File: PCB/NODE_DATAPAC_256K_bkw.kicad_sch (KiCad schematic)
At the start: 28 parts, among them J1 Conn_02x20_Odd_Even, U1 74161, U10 62256, U2 74161, U3 74161, U4 74138, U5 74138, U6 74374, U7 62256, U8 62256, U9 62256

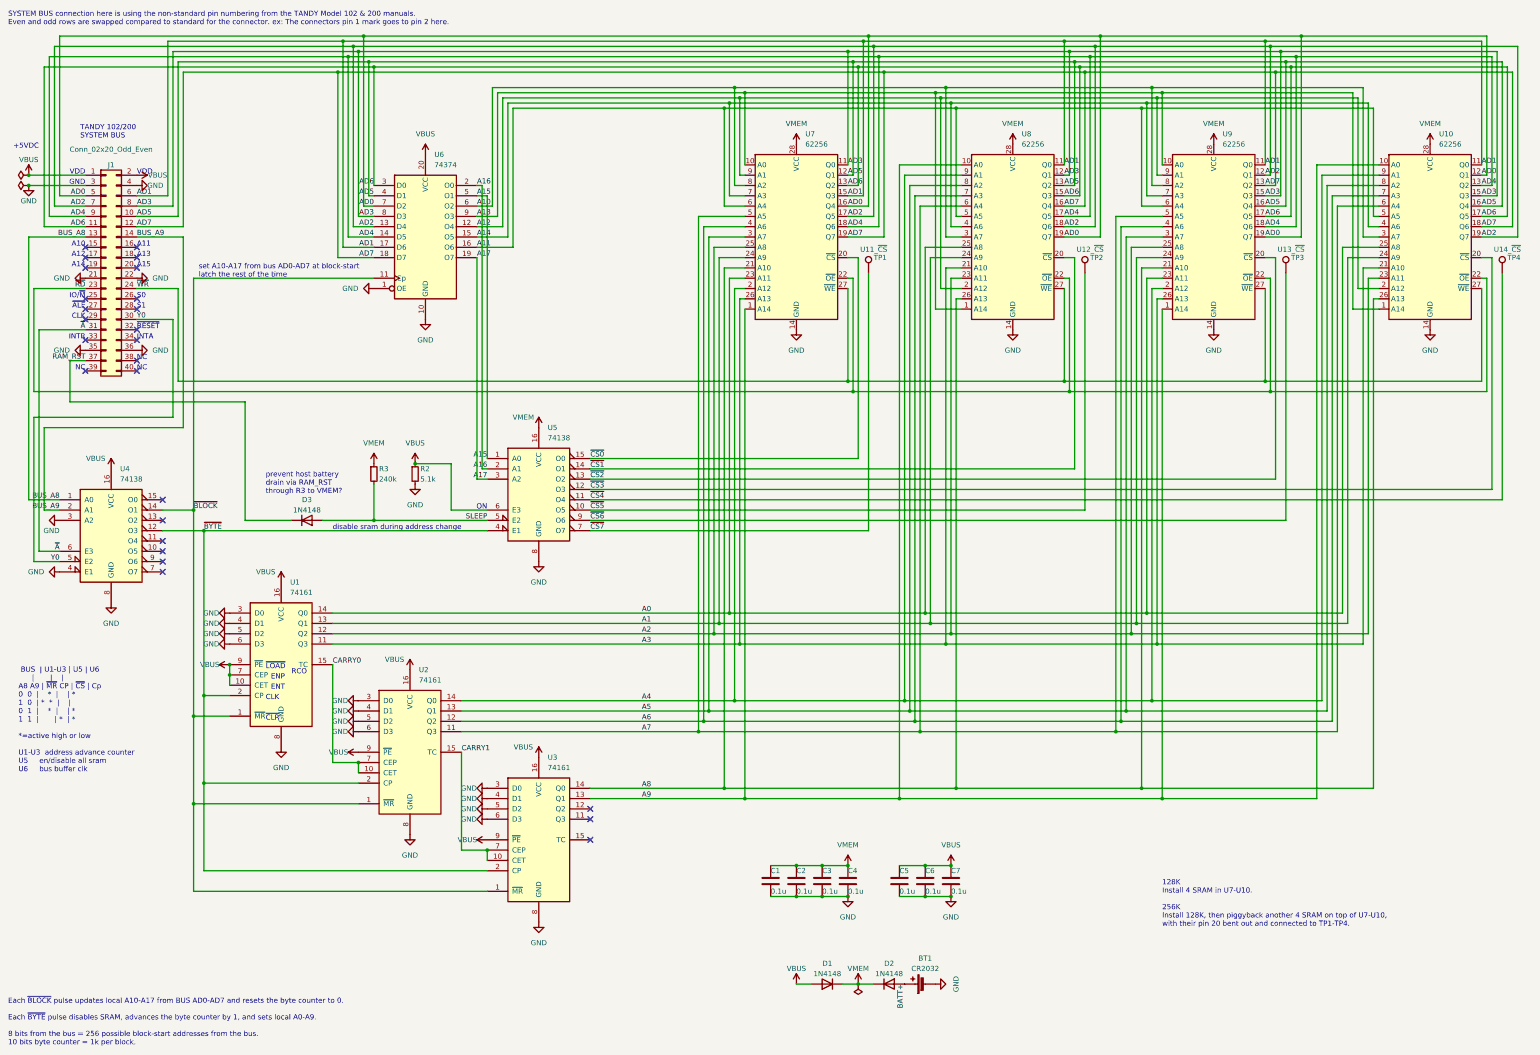
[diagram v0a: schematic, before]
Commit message: convert wires to busses in bkw sch
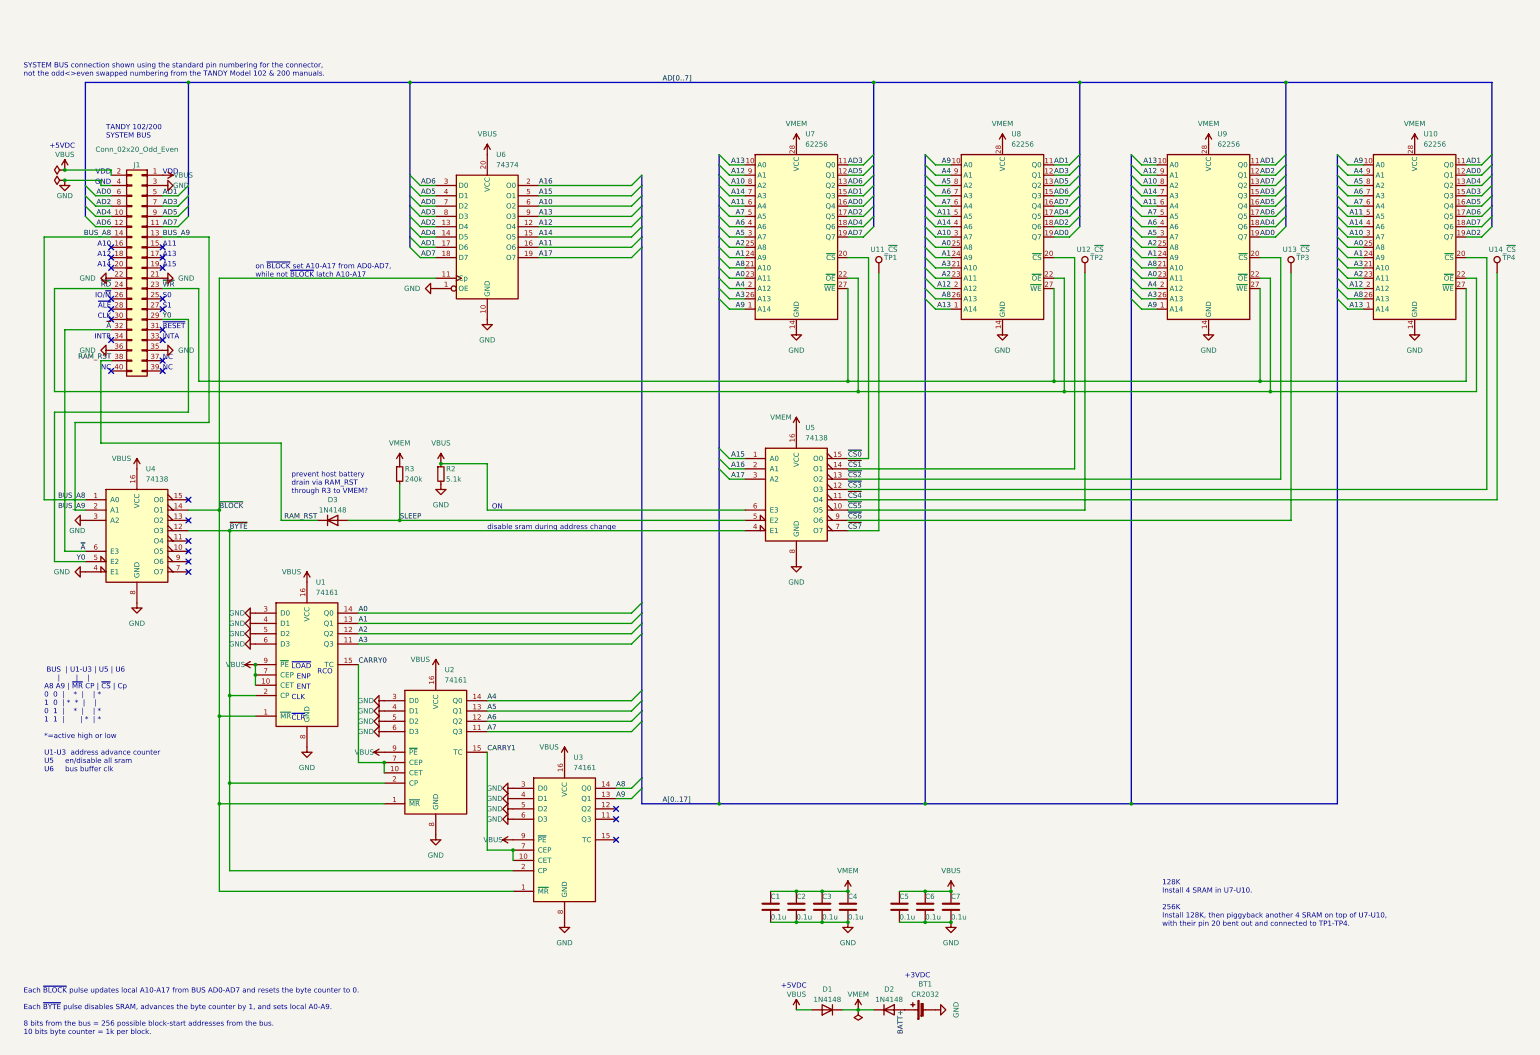
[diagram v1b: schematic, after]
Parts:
- J1: footprint 000_LOCAL:IDC_to_board_2x20_flipped -> 000_LOCAL:IDC_to_board_2x20
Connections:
- net AD0: now also J1.6 (Pin_6); no longer J1.5 (Pin_5)
- net AD1: now also J1.5 (Pin_5); no longer J1.6 (Pin_6)
- net AD2: now also J1.8 (Pin_8); no longer J1.7 (Pin_7)
- net AD3: now also J1.7 (Pin_7); no longer J1.8 (Pin_8)
- net AD4: now also J1.10 (Pin_10); no longer J1.9 (Pin_9)
- net AD5: now also J1.9 (Pin_9); no longer J1.10 (Pin_10)
- net AD6: now also J1.12 (Pin_12); no longer J1.11 (Pin_11)
- net AD7: now also J1.11 (Pin_11); no longer J1.12 (Pin_12)
- net BUS_A8: now also J1.14 (Pin_14); no longer J1.13 (Pin_13)
- net BUS_A9: now also J1.13 (Pin_13); no longer J1.14 (Pin_14)
- net RAM_RST: now also J1.38 (Pin_38); no longer J1.37 (Pin_37)
- net Y0: now also J1.29 (Pin_29); no longer J1.30 (Pin_30)
- net ~{A}: now also J1.32 (Pin_32); no longer J1.31 (Pin_31)
- net ~{RD}: now also J1.24 (Pin_24); no longer J1.23 (Pin_23)
- net ~{WR}: now also J1.23 (Pin_23); no longer J1.24 (Pin_24)
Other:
- note added: "+3VDC"
- note added: "SYSTEM BUS connection shown using the standard pin numbering for the connector, not the odd<>even swapped numbering from the TANDY Model 102 & 200 manuals."
- note added: "on ~{BLOCK} set A10-A17 from AD0-AD7, while not ~{BLOCK} latch A10-A17"
- note removed: "SYSTEM BUS connection here is using the non-standard pin numbering from the TANDY Model 102 & 200 manuals. Even and odd rows are swapped compared to standard for the connector. ex: The connectors pin 1 mark goes to pin 2 here."
- note removed: "set A10-A17 from bus AD0-AD7 at block-start latch the rest of the time"
- title: NODE DATAPAC 256K bkw0 -> NODE DATAPAC 256K bkw
- moved on the sheet: BT1, C1, C2, C3, C4, C5, C6, C7, D1, D2, D3, J1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

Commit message: schematic notes
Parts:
- C1, C2, C3, C4, C5, C6, C7: value 0.1u -> 1u
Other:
- note added: "BUS | U1-U3 | U5 | U6 | | | A8 A9 | ~{MR} CP | ~{CS} | Cp 0 0 | * | | * 1 0 | * * | | 0 1 | * | | * 1 1 | | * | * *=active, whether high or low U1-U3 byte address increment U5 enable/disable sram U6 block address latch"
- note added: "While ~{BLOCK} is low, A0-A9 are set to 0, A10-A17 are copied from AD0-AD7. While ~{BLOCK} is high, A10-A17 are latched and held. While ~{BYTE} is low, SRAM is enabled. When ~{BYTE} goes from low to high, A0-A9 are incremented by 1. While ~{BYTE} is high, SRAM is disabled. A0-A9 = 10 bits byte number = 1024 bytes per block AD0-AD7 -> A10-A17 = 8 bits block number = 256 blocks"
- note removed: "BUS | U1-U3 | U5 | U6 | | | A8 A9 | ~{MR} CP | ~{CS} | Cp 0 0 | * | | * 1 0 | * * | | 0 1 | * | | * 1 1 | | * | * *=active high or low U1-U3 address advance counter U5 en/disable all sram U6 bus buffer clk"
- note removed: "Each ~{BLOCK} pulse updates local A10-A17 from BUS AD0-AD7 and resets the byte counter to 0. Each ~{BYTE} pulse disables SRAM, advances the byte counter by 1, and sets local A0-A9. 8 bits from the bus = 256 possible block-start addresses from the bus. 10 bits byte counter = 1k per block."
- note removed: "disable sram during address change"
- note removed: "on ~{BLOCK} set A10-A17 from AD0-AD7, while not ~{BLOCK} latch A10-A17"

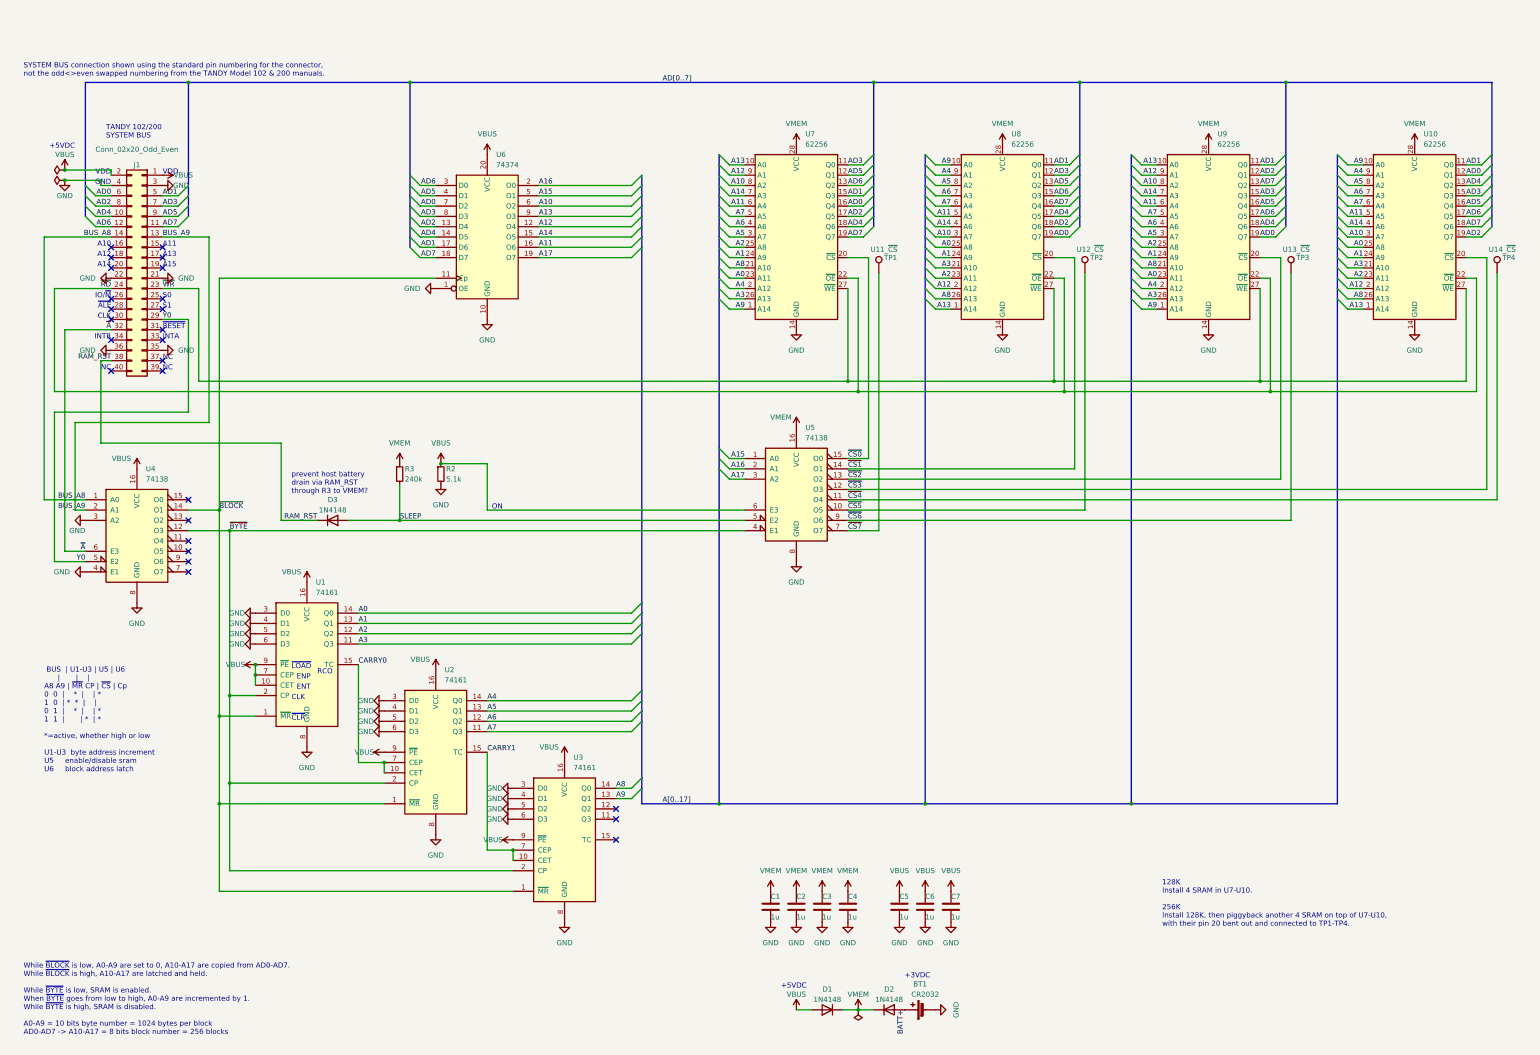
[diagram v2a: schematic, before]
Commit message: fix wrong polarity on net names (A), /Y0, /INTA, INTR, RESET
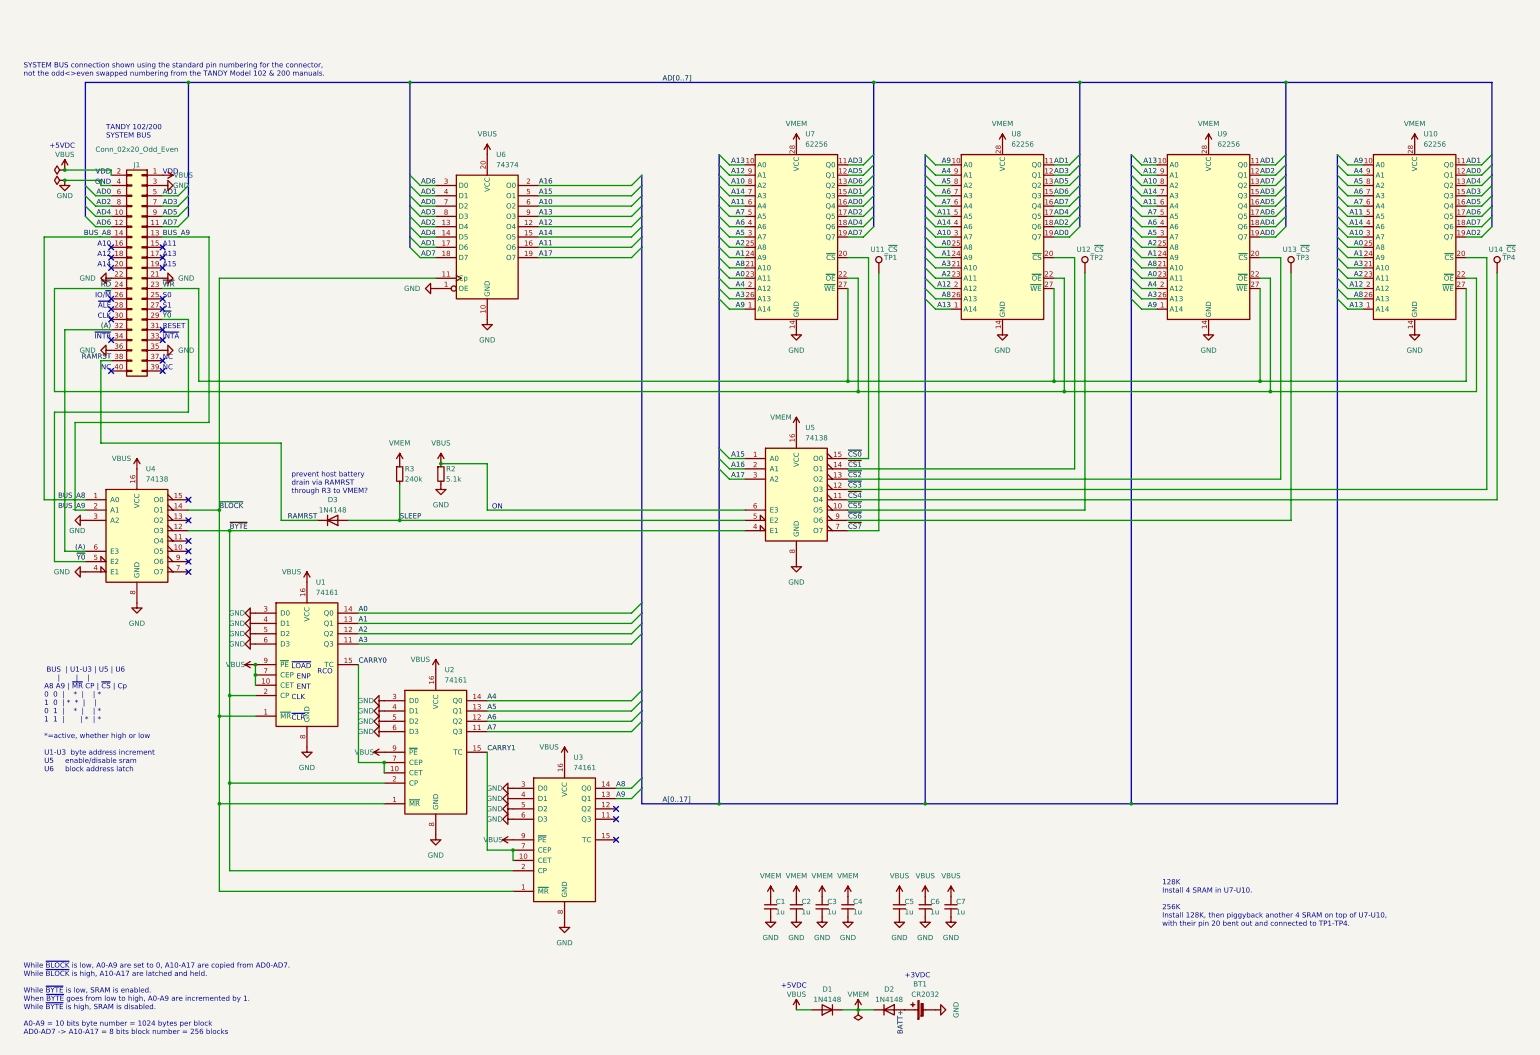
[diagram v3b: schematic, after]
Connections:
- net RAM_RST renamed RAMRST
- net Y0 renamed ~{Y0}
- net ~{A} renamed (A)
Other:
- note added: "RESET"
- note added: "prevent host battery drain via RAMRST through R3 to VMEM?"
- note added: "~{INTA}"
- note added: "~{INTR}"
- note removed: "INTA"
- note removed: "INTR"
- note removed: "prevent host battery drain via RAM_RST through R3 to VMEM?"
- note removed: "~{RESET}"

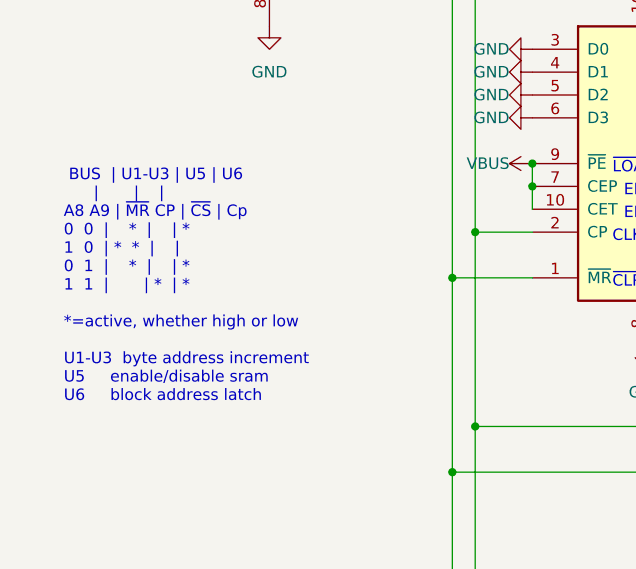
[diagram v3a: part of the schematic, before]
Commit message: remove confusing truth table from sch
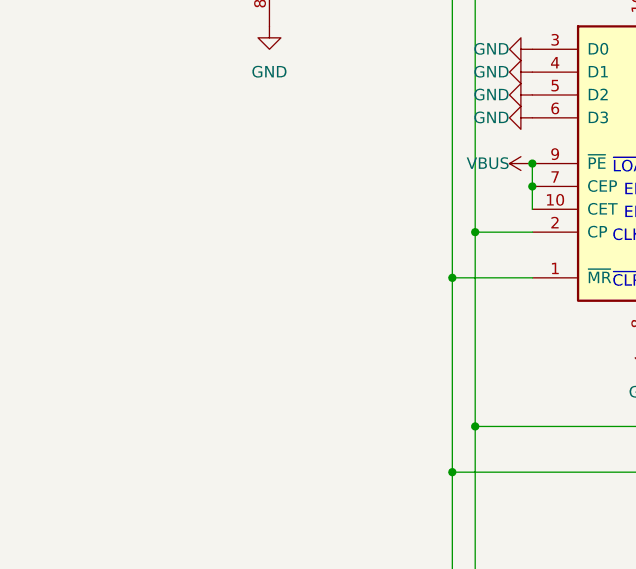
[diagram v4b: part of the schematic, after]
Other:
- note removed: "BUS | U1-U3 | U5 | U6 | | | A8 A9 | ~{MR} CP | ~{CS} | Cp 0 0 | * | | * 1 0 | * * | | 0 1 | * | | * 1 1 | | * | * *=active, whether high or low U1-U3 byte address increment U5 enable/disable sram U6 block address latch"
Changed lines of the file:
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@@
     (effects (font (size 1.27 1.27)) (justify left bottom))
-  )
-  (text " BUS  | U1-U3 | U5 | U6\n      |       |    |\nA8 A9 | ~{MR} CP | ~{CS} | Cp\n0  0  |    *  |    | *\n1  0  | *  *  |    |\n0  1  |    *  |    | *\n1  1  |       | *  | *\n\n*=active, whether high or low\n\nU1-U3  byte address increment\nU5     enable/disable sram\nU6     block address latch"
-    (at 30.48 208.28 0)
-    (effects (font (face "Bitstream Vera Sans Mono") (size 1.27 1.27)) (justify left bottom))
   )
   (text "NC" (at 59.69 106.68 0)

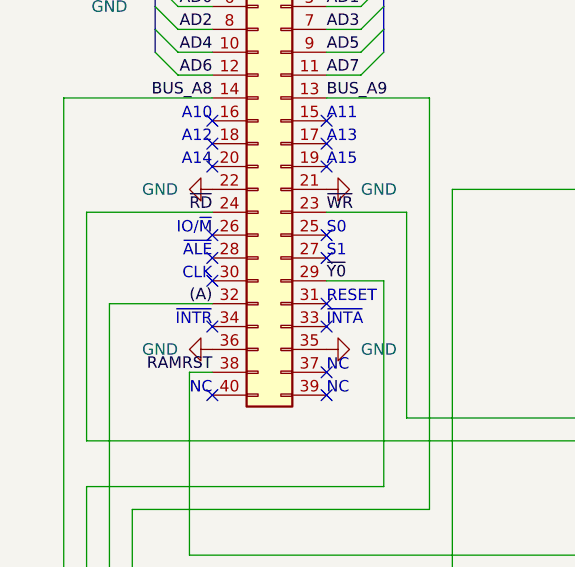
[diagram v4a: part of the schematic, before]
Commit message: fix active-high notation of ALE & INTR in sch comments
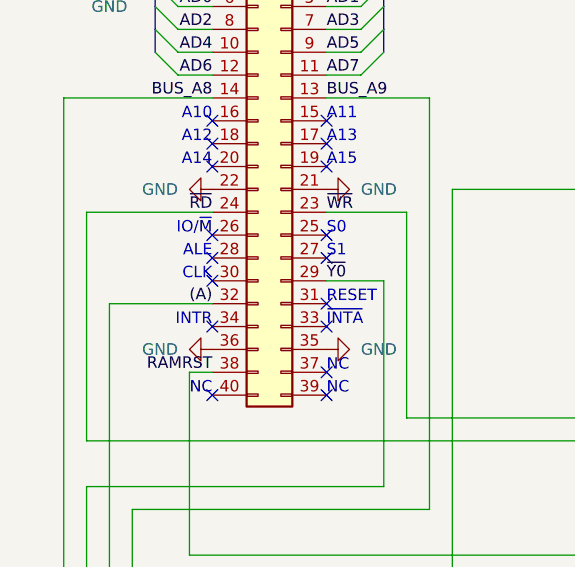
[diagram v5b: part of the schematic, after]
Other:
- note added: "ALE"
- note added: "INTR"
- note removed: "~{ALE}"
- note removed: "~{INTR}"
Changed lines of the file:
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@@
     (effects (font (size 1.27 1.27)) (justify left bottom))
   )
-  (text "~{INTR}" (at 46.99 101.6 0)
+  (text "INTR" (at 46.99 101.6 0)
     (effects (font (size 1.27 1.27)) (justify right bottom))
   )
@@
     (effects (font (size 1.27 1.27)) (justify right bottom))
   )
-  (text "~{ALE}" (at 46.99 93.98 0)
+  (text "ALE" (at 46.99 93.98 0)
     (effects (font (size 1.27 1.27)) (justify right bottom))
   )
